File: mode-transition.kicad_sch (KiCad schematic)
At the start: 4 parts, among them U19001 4081, U19002 4073, U19003 4071, U19004 4069

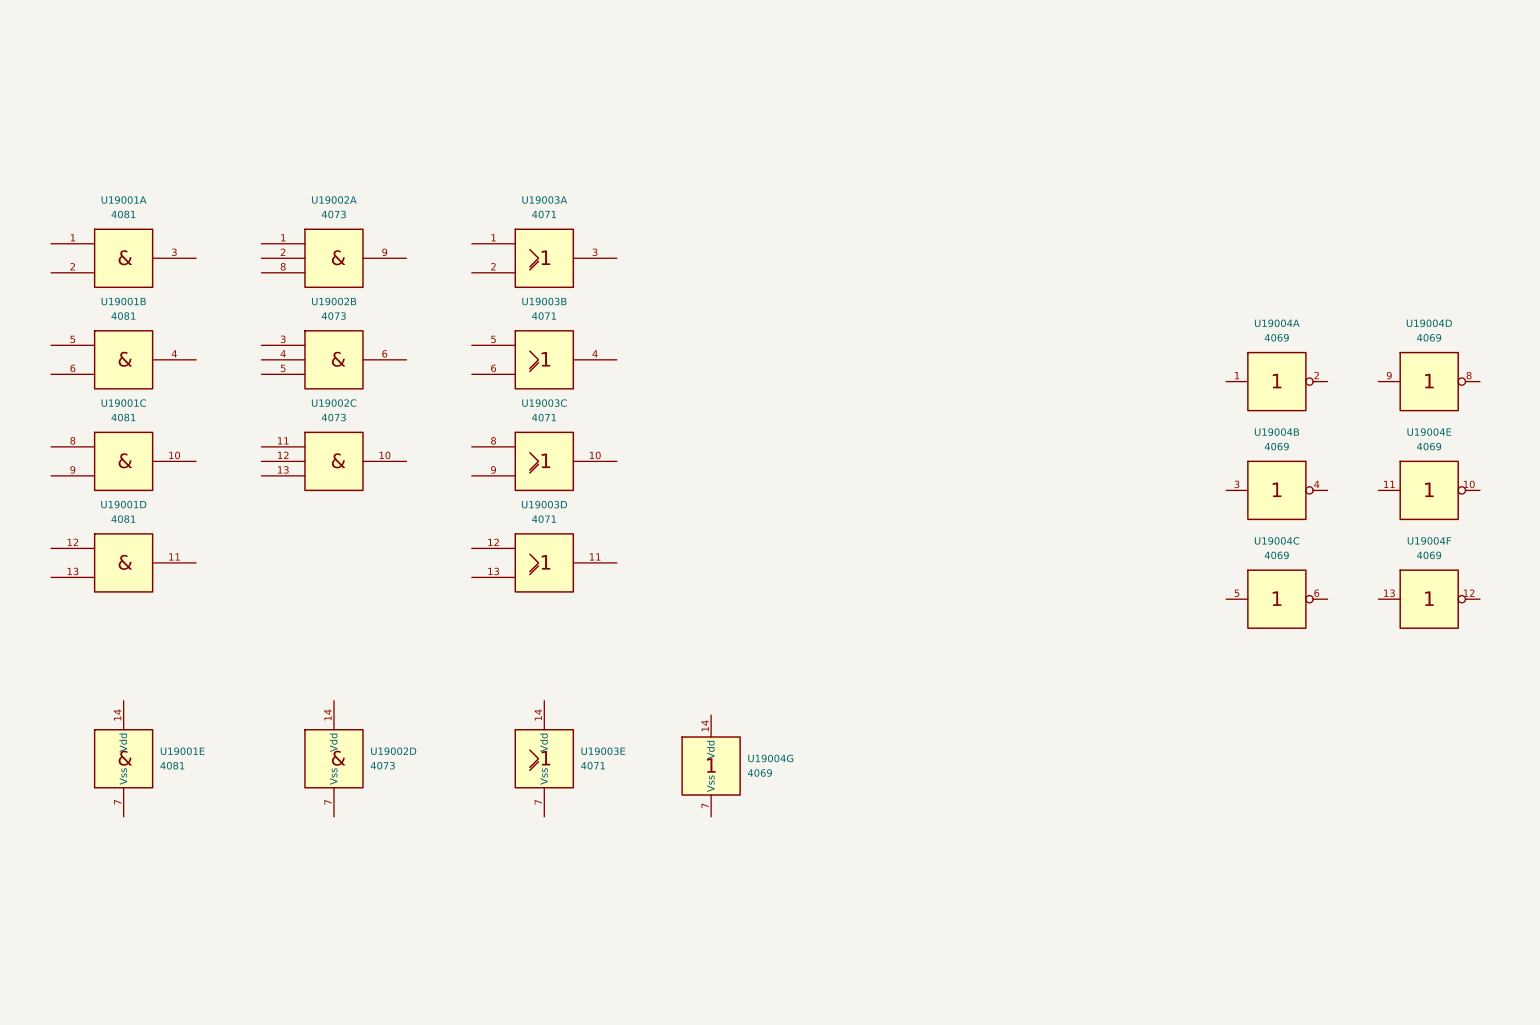
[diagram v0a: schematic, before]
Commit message: add limit-logic mode transition logic
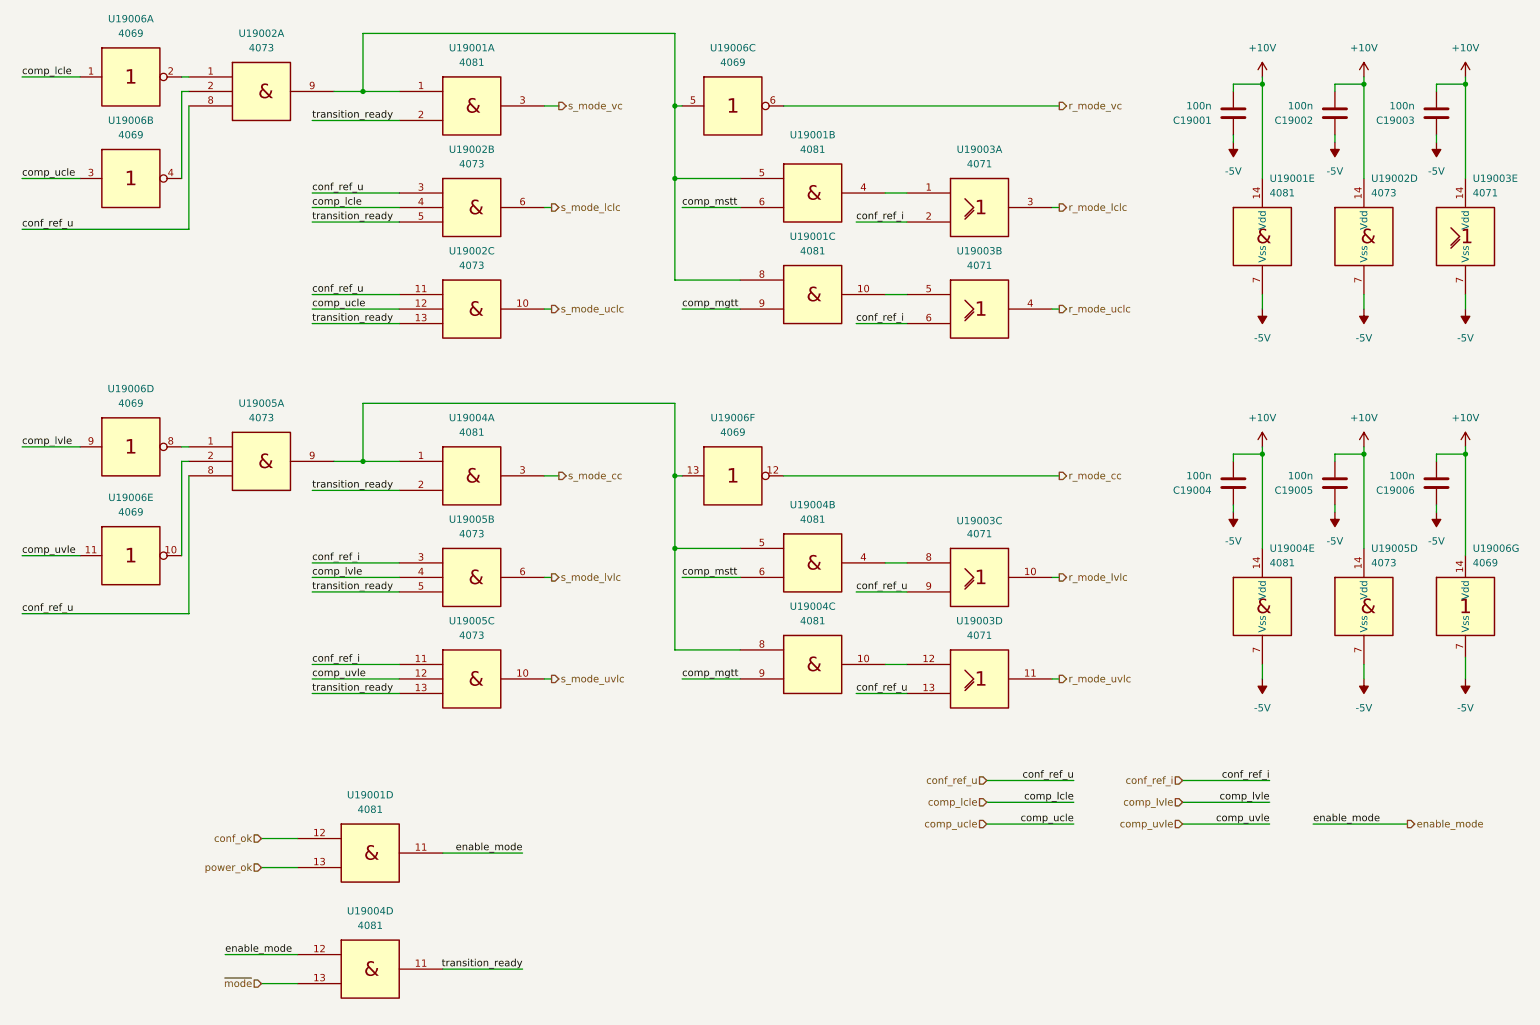
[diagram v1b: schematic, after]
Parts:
- added C19001, C19002, C19003, C19004, C19005, C19006: 100n, Capacitor_SMD:C_0805_2012Metric_Pad1.18x1.45mm_HandSolder, symbol pss:C
- added U19004: 4081, Package_SO:SOIC-14_3.9x8.7mm_P1.27mm, symbol pss:4081
- added U19005: 4073, Package_SO:SOIC-14_3.9x8.7mm_P1.27mm, symbol pss:4073
- renumbered U19004 to U19006
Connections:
- net enable_mode: now reaches U19001.11
- net enable_mode: now also U19004.12
- net conf_ok: now reaches U19001.12
- net power_ok: now reaches U19001.13
- net comp_lcle: now reaches U19006.1
- net comp_lcle: now also U19002.4
- net at U19006.2: now also U19002.1
- net at U19002.2: now also U19006.4
- net conf_ref_u: now reaches U19002.8
- net conf_ref_u: now also U19002.11, U19002.3, U19003.13, U19003.9, U19005.8
- net at U19002.9: now also U19001.1, U19001.5, U19001.8, U19006.5
- net r_mode_vc: now reaches U19006.6
- net +10V: now reaches U19002.14 (Vdd)
- net +10V: now also U19001.14 (Vdd), U19003.14 (Vdd), U19006.14 (Vdd), C19001.2, C19002.2, C19003.2, C19004.2, C19005.2, C19006.2, U19004.14 (Vdd), U19005.14 (Vdd)
- net -5V: now reaches U19002.7 (Vss)
- net -5V: now also U19001.7 (Vss), U19003.7 (Vss), U19006.7 (Vss), C19001.1, C19002.1, C19003.1, C19004.1, C19005.1, C19006.1, U19004.7 (Vss), U19005.7 (Vss)
- net at U19006.8: now also U19005.1
- net comp_lvle: now reaches U19006.9
- net comp_lvle: now also U19005.4
- net r_mode_uvlc: now reaches U19003.11
- net at U19003.12: now also U19004.10
- net r_mode_uclc: now reaches U19003.4
- net at U19003.5: now also U19001.10
- net conf_ref_i: now reaches U19003.6
- net conf_ref_i: now also U19003.2, U19005.11, U19005.3
- net at U19003.1: now also U19001.4
- net r_mode_lclc: now reaches U19003.3
- net comp_mgtt: now reaches U19001.9
- net comp_mgtt: now also U19004.9
- net r_mode_lvlc: now reaches U19003.10
- net at U19003.8: now also U19004.4
- net comp_ucle: now reaches U19006.3
- net comp_ucle: now also U19002.12
- net transition_ready: now reaches U19002.5
- net transition_ready: now also U19001.2, U19002.13, U19004.11, U19004.2, U19005.13, U19005.5
- net s_mode_lclc: now reaches U19002.6
- net s_mode_vc: now reaches U19001.3
- net r_mode_cc: now reaches U19006.12
- net at U19006.13: now also U19004.1, U19004.5, U19004.8, U19005.9
- net s_mode_uclc: now reaches U19002.10
- net at U19006.10: now also U19005.2
- net comp_uvle: now reaches U19006.11
- net comp_uvle: now also U19005.12
- net comp_mstt: now reaches U19001.6
- net comp_mstt: now also U19004.6
- new net s_mode_cc: U19004.3
- new net s_mode_lvlc: U19005.6
- new net s_mode_uvlc: U19005.10
- new net ~{mode}: U19004.13
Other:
- moved on the sheet: U19001A, U19001B, U19001C, U19001D, U19001E, U19002A, U19002B, U19002C, U19002D, U19003A, U19003B, U19003C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

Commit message: add limit-logic start up state pull downs
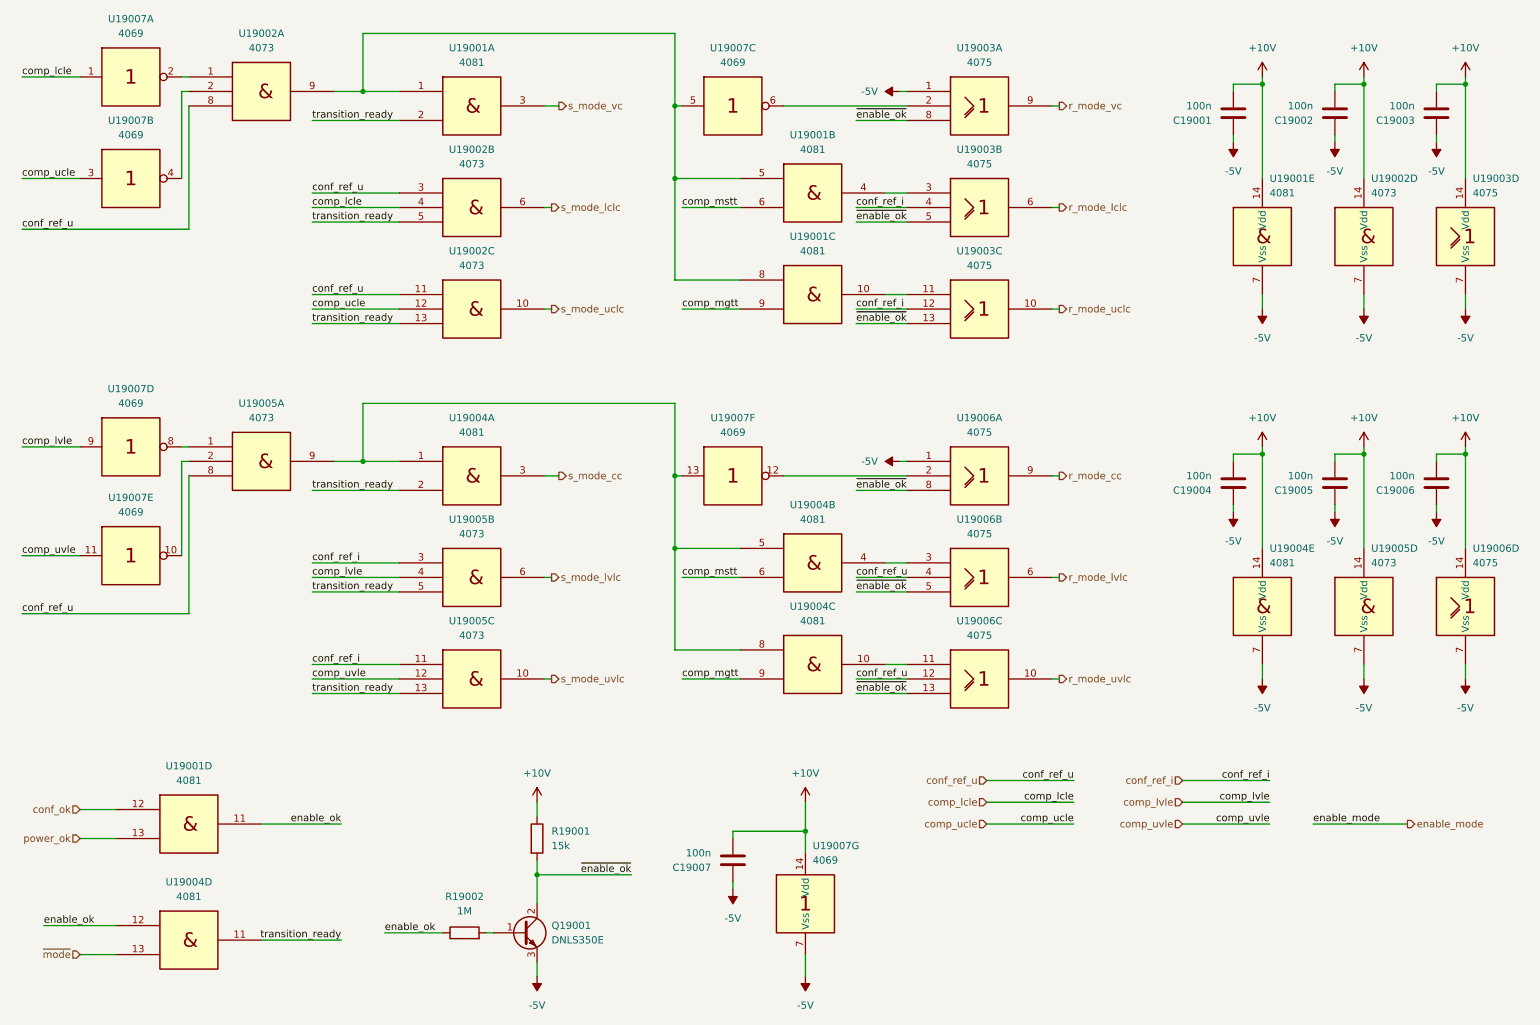
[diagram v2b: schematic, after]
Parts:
- removed U19003: 4071, Package_SO:SOIC-14_3.9x8.7mm_P1.27mm, symbol pss:4071
- added C19006: 100n, Capacitor_SMD:C_0805_2012Metric_Pad1.18x1.45mm_HandSolder, symbol pss:C
- added Q19001: DNLS350E, symbol pss:Q_NPN_BCE
- added R19001: 15k, Resistor_SMD:R_1210_3225Metric_Pad1.30x2.65mm_HandSolder, symbol pss:R
- added R19002: 1M, Resistor_SMD:R_1210_3225Metric_Pad1.30x2.65mm_HandSolder, symbol pss:R
- added U19003, U19006: 4075, symbol pss:4075
- renumbered C19006 to C19007, U19006 to U19007
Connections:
- net +10V: now also C19006.2, R19001.1, U19003.14 (Vdd), U19006.14 (Vdd)
- net -5V: now also C19006.1, Q19001.3 (E), U19003.1, U19003.7 (Vss), U19006.1, U19006.7 (Vss)
- net conf_ref_i: now also U19003.12, U19003.4
- net conf_ref_u: now also U19006.12, U19006.4
- net enable_mode: no longer U19001.11, U19004.12
- net r_mode_cc: now also U19006.9; no longer U19007.12
- net r_mode_lclc: now also U19003.6
- net r_mode_lvlc: now also U19006.6
- net r_mode_uclc: now also U19003.10
- net r_mode_uvlc: now also U19006.10
- net r_mode_vc: now also U19003.9; no longer U19007.6
- net at U19004.10: now also U19006.11
- net at U19001.10: now also U19003.11
- net at U19001.4: now also U19003.3
- net at U19004.4: now also U19006.3
- new net: U19003.2, U19007.6
- new net: U19006.2, U19007.12
- new net: Q19001.1 (B), R19002.2
- new net enable_ok: R19002.1, U19001.11, U19004.12
- new net ~{enable_ok}: Q19001.2 (C), R19001.2, U19003.13, U19003.5, U19003.8, U19006.13, U19006.5, U19006.8
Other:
- moved on the sheet: C19007, U19001D, U19004D, U19007G

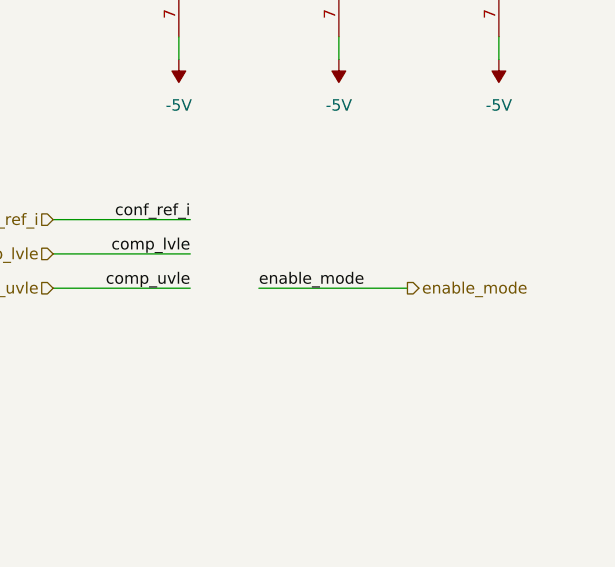
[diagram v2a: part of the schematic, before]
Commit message: add limit-logic pull ups for tristate of mode latches
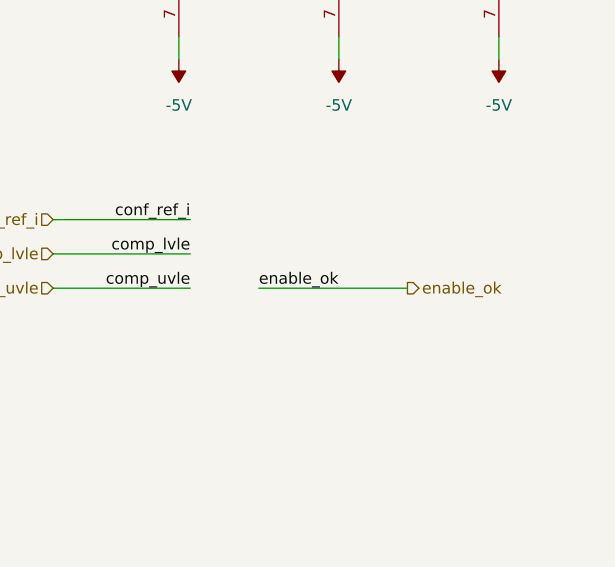
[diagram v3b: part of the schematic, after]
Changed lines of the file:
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@@
 		)
 	)
-	(label "enable_mode"
+	(label "enable_ok"
 		(at 246.38 160.02 0)
 		(fields_autoplaced yes)
@@
 		)
 	)
-	(hierarchical_label "enable_mode"
+	(hierarchical_label "enable_ok"
 		(shape output)
 		(at 262.89 160.02 0)
